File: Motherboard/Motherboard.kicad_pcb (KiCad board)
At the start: 8 copper layers, 304.8 x 243.8 mm, 110 parts, among them J1 ATX-20, J2 65SIB_Connector, J3 DB9_Header, J4 GPIO_Connector, J5 Expansion_Connector, J6 Expansion_Connector, J7 Expansion_Connector, J8 Expansion_Connector, J9 Expansion_Connector, SW1 SW_SPST, U1 74HCT138, U10 74HCT138, U11 74HCT02, U2 AS6C4008-55PCN, U3 74HCT138, U4 74HCT138, U5 74HCT138, U6 28C010, U7 74HCT08, U8 74HCT138, U9 74HCT138, X1 ACO-8MHz

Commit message: 214 unrouted traces...
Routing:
- net A11: track 46.2 -> 152.5 mm
- net A10: track 46.2 -> 152.5 mm
- net CS_DEV: track 300.6 -> 406.8 mm
- net 8MHz: track 304.0 -> 410.2 mm
- net A13: track 0.00 -> 54.5 mm, vias 0 -> 2
- net A14: track 0.00 -> 52.1 mm, vias 0 -> 2
- net A15: track 0.00 -> 49.6 mm, vias 0 -> 2
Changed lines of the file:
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@@
   (via (at 132.08 128.27) (size 0.8) (drill 0.4) (layers "F.Cu" "B.Cu") (net 23))
   (via (at 153.67 209.55) (size 0.8) (drill 0.4) (layers "F.Cu" "B.Cu") (net 23))
+  (segment (start 228.59 64.77) (end 251.47 64.77) (width 0.25) (layer "In2.Cu") (net 23))
+  (segment (start 226.07 64.77) (end 227.33 63.51) (width 0.25) (layer "In2.Cu") (net 23))
+  (segment (start 279.4 64.755) (end 302.725 64.755) (width 0.25) (layer "In2.Cu") (net 23))
+  (segment (start 278.13 63.485) (end 279.4 64.755) (width 0.25) (layer "In2.Cu") (net 23))
+  (segment (start 251.47 64.77) (end 252.73 63.51) (width 0.25) (layer "In2.Cu") (net 23))
   (segment (start 132.08 128.27) (end 132.08 220.98) (width 0.25) (layer "In2.Cu") (net 23))
+  (segment (start 302.725 64.755) (end 303.98 63.5) (width 0.25) (layer "In2.Cu") (net 23))
   (segment (start 153.67 209.55) (end 153.67 219.71) (width 0.25) (layer "In2.Cu") (net 23))
+  (segment (start 203.2 64.77) (end 226.07 64.77) (width 0.25) (layer "In2.Cu") (net 23))
+  (segment (start 252.73 63.51) (end 253.99 64.77) (width 0.25) (layer "In2.Cu") (net 23))
+  (segment (start 201.93 63.5) (end 203.2 64.77) (width 0.25) (layer "In2.Cu") (net 23))
   (segment (start 132.08 128.27) (end 132.08 115.57) (width 0.25) (layer "In2.Cu") (net 23))
   (segment (start 114.3 87.63) (end 114.3 128.27) (width 0.25) (layer "In2.Cu") (net 23))
+  (segment (start 227.33 63.51) (end 228.59 64.77) (width 0.25) (layer "In2.Cu") (net 23))
+  (segment (start 253.99 64.77) (end 276.845 64.77) (width 0.25) (layer "In2.Cu") (net 23))
+  (segment (start 276.845 64.77) (end 278.13 63.485) (width 0.25) (layer "In2.Cu") (net 23))
   (segment (start 146.05 220.98) (end 147.32 219.71) (width 0.25) (layer "In3.Cu") (net 23))
   (segment (start 114.3 128.27) (end 132.08 128.27) (width 0.25) (layer "In3.Cu") (net 23))
@@
   (via (at 85.09 226.06) (size 0.8) (drill 0.4) (layers "F.Cu" "B.Cu") (net 53))
   (via (at 102.87 209.55) (size 0.8) (drill 0.4) (layers "F.Cu" "B.Cu") (net 53))
+  (segment (start 253.99 62.23) (end 276.845 62.23) (width 0.25) (layer "In2.Cu") (net 53))
+  (segment (start 201.93 60.96) (end 203.104511 62.134511) (width 0.25) (layer "In2.Cu") (net 53))
   (segment (start 102.87 199.39) (end 102.87 209.55) (width 0.25) (layer "In2.Cu") (net 53))
   (segment (start 186.69 64.77) (end 186.69 60.96) (width 0.25) (layer "In2.Cu") (net 53))
+  (segment (start 203.104511 62.134511) (end 226.165489 62.134511) (width 0.25) (layer "In2.Cu") (net 53))
+  (segment (start 227.33 60.97) (end 228.504511 62.144511) (width 0.25) (layer "In2.Cu") (net 53))
+  (segment (start 226.165489 62.134511) (end 227.33 60.97) (width 0.25) (layer "In2.Cu") (net 53))
   (segment (start 114.3 209.55) (end 115.57 208.28) (width 0.25) (layer "In2.Cu") (net 53))
+  (segment (start 278.13 60.945) (end 279.415 62.23) (width 0.25) (layer "In2.Cu") (net 53))
+  (segment (start 228.504511 62.144511) (end 251.555489 62.144511) (width 0.25) (layer "In2.Cu") (net 53))
   (segment (start 115.57 208.28) (end 115.57 64.77) (width 0.25) (layer "In2.Cu") (net 53))
+  (segment (start 279.415 62.23) (end 302.71 62.23) (width 0.25) (layer "In2.Cu") (net 53))
+  (segment (start 276.845 62.23) (end 278.13 60.945) (width 0.25) (layer "In2.Cu") (net 53))
+  (segment (start 302.71 62.23) (end 303.98 60.96) (width 0.25) (layer "In2.Cu") (net 53))
   (segment (start 85.09 226.06) (end 85.09 208.28) (width 0.25) (layer "In2.Cu") (net 53))
+  (segment (start 252.73 60.97) (end 253.99 62.23) (width 0.25) (layer "In2.Cu") (net 53))
+  (segment (start 251.555489 62.144511) (end 252.73 60.97) (width 0.25) (layer "In2.Cu") (net 53))
   (segment (start 102.87 209.55) (end 114.3 209.55) (width 0.25) (layer "In3.Cu") (net 53))
   (segment (start 85.09 208.28) (end 85.085 208.275) (width 0.25) (layer "In3.Cu") (net 53))
@@
   (segment (start 280.1275 162.56) (end 278.8575 163.83) (width 0.25) (layer "In2.Cu") (net 70))
   (segment (start 278.8575 163.83) (end 236.215 163.83) (width 0.25) (layer "In2.Cu") (net 70))
+  (segment (start 279.385 62.23) (end 280.67 60.945) (width 0.25) (layer "In3.Cu") (net 70))
+  (segment (start 228.61 62.23) (end 229.87 60.97) (width 0.25) (layer "In3.Cu") (net 70))
+  (segment (start 205.74 62.23) (end 228.61 62.23) (width 0.25) (layer "In3.Cu") (net 70))
+  (segment (start 305.265 62.215) (end 306.52 60.96) (width 0.25) (layer "In3.Cu") (net 70))
+  (segment (start 280.67 60.945) (end 281.94 62.215) (width 0.25) (layer "In3.Cu") (net 70))
+  (segment (start 255.27 60.97) (end 256.53 62.23) (width 0.25) (layer "In3.Cu") (net 70))
+  (segment (start 281.94 62.215) (end 305.265 62.215) (width 0.25) (layer "In3.Cu") (net 70))
+  (segment (start 256.53 62.23) (end 279.385 62.23) (width 0.25) (layer "In3.Cu") (net 70))
+  (segment (start 254.01 62.23) (end 255.27 60.97) (width 0.25) (layer "In3.Cu") (net 70))
+  (segment (start 204.47 60.96) (end 205.74 62.23) (width 0.25) (layer "In3.Cu") (net 70))
+  (segment (start 231.13 62.23) (end 254.01 62.23) (width 0.25) (layer "In3.Cu") (net 70))
+  (segment (start 229.87 60.97) (end 231.13 62.23) (width 0.25) (layer "In3.Cu") (net 70))
   (segment (start 236.215 158.75) (end 234.945 157.48) (width 0.25) (layer "In2.Cu") (net 71))
   (segment (start 280.1275 157.48) (end 278.8575 158.75) (width 0.25) (layer "In2.Cu") (net 71))
   (segment (start 278.8575 158.75) (end 236.215 158.75) (width 0.25) (layer "In2.Cu") (net 71))
+  (segment (start 231.13 64.77) (end 254.01 64.77) (width 0.25) (layer "In3.Cu") (net 71))
+  (segment (start 306.52 63.5) (end 305.25 64.77) (width 0.25) (layer "In3.Cu") (net 71))
+  (segment (start 229.87 63.51) (end 231.13 64.77) (width 0.25) (layer "In3.Cu") (net 71))
+  (segment (start 255.27 63.51) (end 256.53 64.77) (width 0.25) (layer "In3.Cu") (net 71))
+  (segment (start 228.61 64.77) (end 229.87 63.51) (width 0.25) (layer "In3.Cu") (net 71))
+  (segment (start 204.47 63.5) (end 205.74 64.77) (width 0.25) (layer "In3.Cu") (net 71))
+  (segment (start 205.74 64.77) (end 228.61 64.77) (width 0.25) (layer "In3.Cu") (net 71))
+  (segment (start 256.53 64.77) (end 279.385 64.77) (width 0.25) (layer "In3.Cu") (net 71))
+  (segment (start 254.01 64.77) (end 255.27 63.51) (width 0.25) (layer "In3.Cu") (net 71))
+  (segment (start 305.25 64.77) (end 281.955 64.77) (width 0.25) (layer "In3.Cu") (net 71))
+  (segment (start 281.955 64.77) (end 280.67 63.485) (width 0.25) (layer "In3.Cu") (net 71))
+  (segment (start 279.385 64.77) (end 280.67 63.485) (width 0.25) (layer "In3.Cu") (net 71))
   (segment (start 263.762989 148.444511) (end 264.8875 147.32) (width 0.25) (layer "In3.Cu") (net 72))
   (segment (start 219.705 147.32) (end 220.829511 148.444511) (width 0.25) (layer "In3.Cu") (net 72))
   (segment (start 220.829511 148.444511) (end 263.762989 148.444511) (width 0.25) (layer "In3.Cu") (net 72))
+  (segment (start 96.53 88.89) (end 102.88 88.89) (width 0.25) (layer "F.Cu") (net 73))
+  (segment (start 96.52 88.9) (end 96.53 88.89) (width 0.25) (layer "F.Cu") (net 73))
+  (via (at 96.702 114.3) (size 0.8) (drill 0.4) (layers "F.Cu" "B.Cu") (net 73))
+  (via (at 96.52 88.9) (size 0.8) (drill 0.4) (layers "F.Cu" "B.Cu") (net 73))
+  (segment (start 96.702 89.082) (end 96.52 88.9) (width 0.25) (layer "In2.Cu") (net 73))
+  (segment (start 96.702 114.3) (end 96.702 89.082) (width 0.25) (layer "In2.Cu") (net 73))
+  (segment (start 96.712 114.29) (end 96.702 114.3) (width 0.25) (layer "In3.Cu") (net 73))
+  (segment (start 119.39 114.29) (end 96.712 114.29) (width 0.25) (layer "In3.Cu") (net 73))
+  (via (at 97.79 91.44) (size 0.8) (drill 0.4) (layers "F.Cu" "B.Cu") (net 74))
+  (via (at 97.79 116.84) (size 0.8) (drill 0.4) (layers "F.Cu" "B.Cu") (net 74))
+  (segment (start 97.79 91.44) (end 97.79 116.84) (width 0.25) (layer "In2.Cu") (net 74))
+  (segment (start 97.8 116.83) (end 119.39 116.83) (width 0.25) (layer "In3.Cu") (net 74))
+  (segment (start 102.88 91.43) (end 97.8 91.43) (width 0.25) (layer "In3.Cu") (net 74))
+  (segment (start 97.79 116.84) (end 97.8 116.83) (width 0.25) (layer "In3.Cu") (net 74))
+  (segment (start 97.8 91.43) (end 97.79 91.44) (width 0.25) (layer "In3.Cu") (net 74))
+  (segment (start 100.33 99.06) (end 100.34 99.05) (width 0.25) (layer "F.Cu") (net 75))
+  (via (at 100.33 127) (size 0.8) (drill 0.4) (layers "F.Cu" "B.Cu") (net 75))
+  (via (at 100.33 99.06) (size 0.8) (drill 0.4) (layers "F.Cu" "B.Cu") (net 75))
+  (segment (start 100.33 99.06) (end 100.33 127) (width 0.25) (layer "In2.Cu") (net 75))
+  (segment (start 102.88 99.05) (end 100.34 99.05) (width 0.25) (layer "In3.Cu") (net 75))
+  (segment (start 100.34 126.99) (end 100.33 127) (width 0.25) (layer "In3.Cu") (net 75))
+  (segment (start 119.39 126.99) (end 100.34 126.99) (width 0.25) (layer "In3.Cu") (net 75))
+  (segment (start 100.34 99.05) (end 100.33 99.06) (width 0.25) (layer "In3.Cu") (net 75))
   (via (at 45.72 124.46) (size 0.8) (drill 0.4) (layers "F.Cu" "B.Cu") (net 85))
   (via (at 45.72 138.43) (size 0.8) (drill 0.4) (layers "F.Cu" "B.Cu") (net 85))

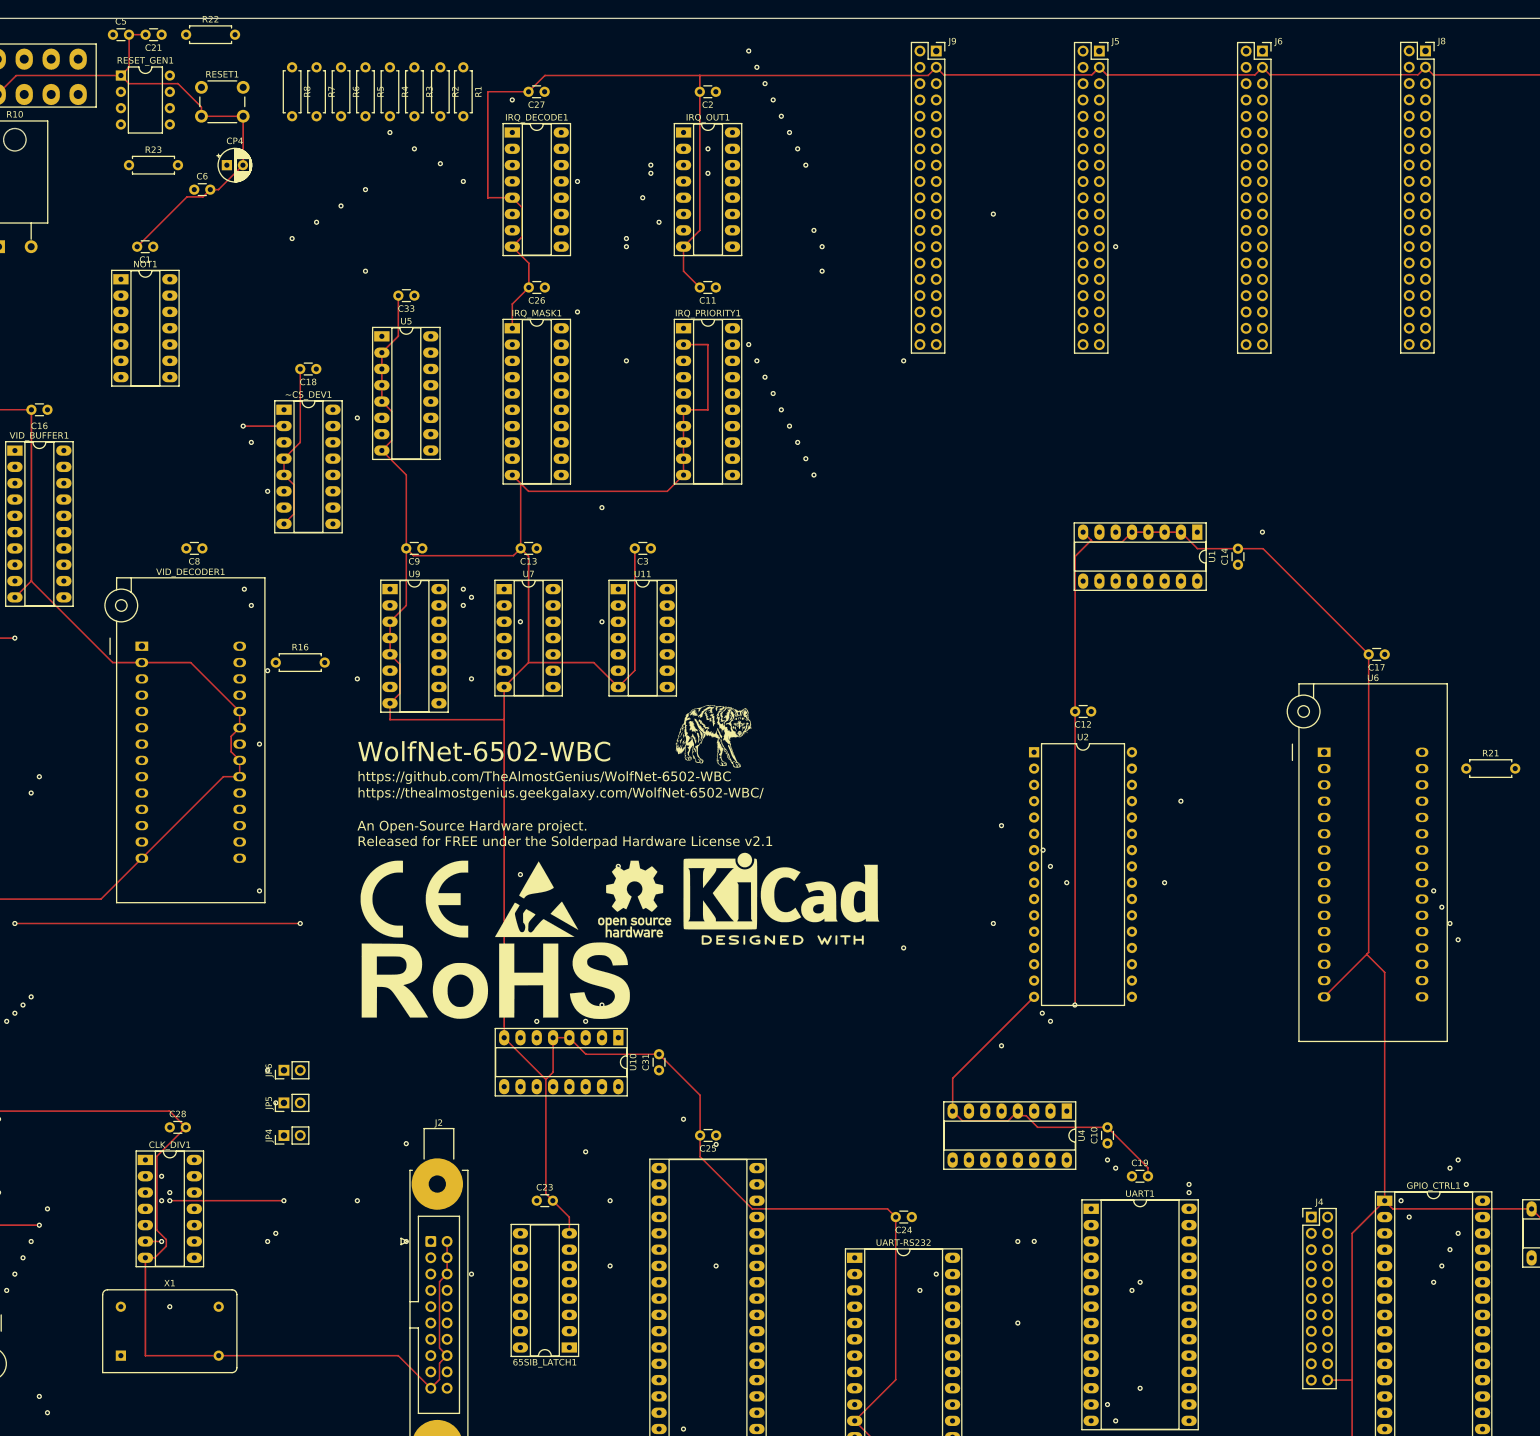
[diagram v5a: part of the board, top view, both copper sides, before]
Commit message: 173 unrouted traces...
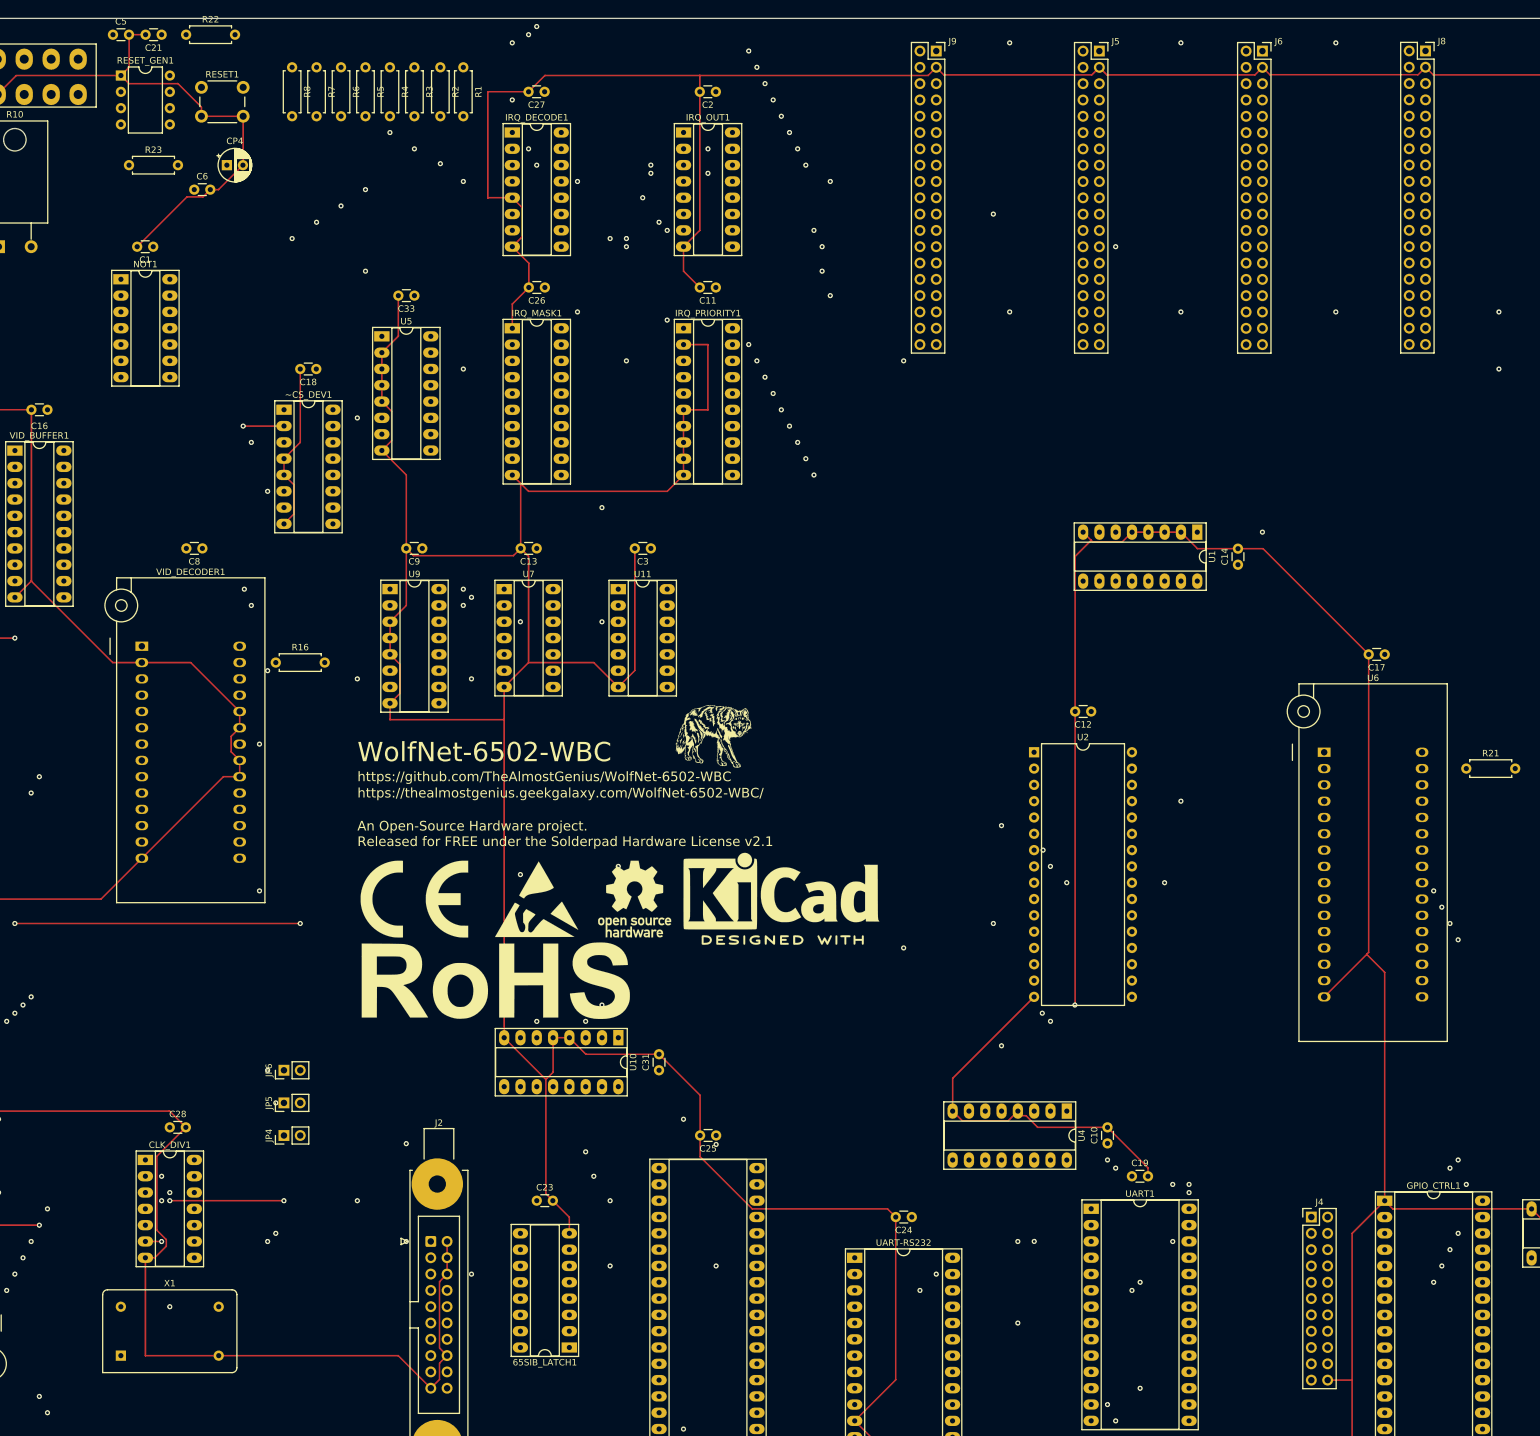
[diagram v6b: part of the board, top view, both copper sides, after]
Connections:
- J7 pad 34: ~{IRQ6} -> ~{IRQ7}
- J8 pad 34: ~{IRQ7} -> ~{IRQ6}
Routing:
- net ~{IRQ0}: track 62.2 -> 319.1 mm, vias 1 -> 5
- net ~{IRQ7}: track 17.8 -> 229.1 mm, vias 1 -> 4
- net ~{IRQ6}: track 18.7 -> 222.9 mm, vias 1 -> 5
- net ~{IRQ5}: track 20.3 -> 195.8 mm, vias 1 -> 5
- net ~{RESET}: track 106.2 -> 249.4 mm, vias 0 -> 2
- net ~{IRQ4}: track 26.7 -> 166.4 mm, vias 2 -> 5
- net A14: track 52.1 -> 158.4 mm
- net SYNC: track 0.00 -> 106.3 mm
- net R\~{W}: track 323.8 -> 430.1 mm
- net A13: track 54.5 -> 160.8 mm
- net A12: track 46.1 -> 152.3 mm
- net +12v: track 468.8 -> 574.9 mm
- net RDY: track 3.81 -> 110.0 mm
- net A15: track 49.6 -> 155.7 mm
- net Net-(IRQ_OUT1-Pad7): track 0.00 -> 103.2 mm, vias 0 -> 2
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
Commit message: 157 unrouted traces...
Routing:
- net ~{RESET}: track 249.4 -> 563.1 mm, vias 2 -> 10
- net ROM1_EN: track 0.00 -> 215.4 mm, vias 0 -> 4
- net ROM2_EN: track 0.00 -> 215.4 mm, vias 0 -> 4
- net MEM_D1: track 346.3 -> 544.3 mm, vias 2 -> 5
- net ~{IRQ}: track 0.00 -> 95.8 mm, vias 0 -> 1
- net DCD_COM: track 0.00 -> 42.0 mm
- net Rx_COM: track 0.00 -> 39.4 mm
- net RTS_COM: track 0.00 -> 38.9 mm
- net Tx_COM: track 0.00 -> 38.8 mm
- net CTS_COM: track 0.00 -> 37.8 mm
- net Net-(IRQ_DECODE1-Pad7): track 72.2 -> 36.4 mm
- net CPU_D1: track 0.00 -> 34.6 mm
- net CPU_D0: track 0.00 -> 34.6 mm
- net CPU_D2: track 0.00 -> 34.2 mm, vias 0 -> 1
- net RTS_COM_PORT: track 33.9 -> 38.4 mm

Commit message: 149 unrouted traces...
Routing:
- net MEM_D0: track 485.2 -> 671.9 mm, vias 4 -> 11
- net MEM_D2: track 263.8 -> 439.0 mm, vias 2 -> 7
- net MEM_D1: track 544.3 -> 670.0 mm, vias 5 -> 9
- net CS_DEV: track 406.8 -> 530.0 mm, vias 7 -> 11
- net A10: track 152.5 -> 272.4 mm, vias 0 -> 2
- net A11: track 152.5 -> 266.1 mm, vias 0 -> 2
